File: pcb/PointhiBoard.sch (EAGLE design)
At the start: 99 parts, among them IC1 MCP7940NMSOP8, IC2 ADP2303ARDZ-5.0, IC3 IRF7240, IC4 IRF7240, IC6 4052D, IC7 ADR02, J1 22-27-2021-02, Q1 BSS123, Q2 BSS123, Q3 BSS123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

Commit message: fix wrong adc-port, little layout modifies
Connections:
- removed net RA4: IC5.RA4/T0CKI/C1OUT, R26.2
- new net AN4: IC5.RA5/AN4/HLVDIN/C2OUT, R26.2
- net N$60: now also IC5.RE1/WRN_AN6; no longer IC5.RA5/AN4/HLVDIN/C2OUT
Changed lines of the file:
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@@
-</segment>
-</net>
-<net name="RA4" class="0">
-<segment>
-<pinref part="IC5" gate="G$1" pin="RA4/T0CKI/C1OUT"/>
-<wire x1="254" y1="-142.24" x2="223.52" y2="-142.24" width="0.1524" layer="91"/>
-<label x="223.52" y="-142.24" size="1.778" layer="95" rot="R180" xref="yes"/>
-</segment>
-<segment>
-<pinref part="R26" gate="G$1" pin="2"/>
-<wire x1="558.8" y1="-132.08" x2="553.72" y2="-132.08" width="0.1524" layer="91"/>
-<label x="553.72" y="-132.08" size="1.778" layer="95" rot="R180" xref="yes"/>
 </segment>
 </net>
@@
 <net name="N$60" class="0">
 <segment>
-<pinref part="IC5" gate="G$1" pin="RA5/AN4/HLVDIN/C2OUT"/>
-<wire x1="254" y1="-147.32" x2="223.52" y2="-147.32" width="0.1524" layer="91"/>
 <pinref part="R31" gate="G$1" pin="1"/>
-<wire x1="223.52" y1="-147.32" x2="223.52" y2="-172.72" width="0.1524" layer="91"/>
 <wire x1="223.52" y1="-172.72" x2="142.24" y2="-172.72" width="0.1524" layer="91"/>
 <wire x1="142.24" y1="-172.72" x2="142.24" y2="-170.18" width="0.1524" layer="91"/>
@@
 <wire x1="142.24" y1="-175.26" x2="142.24" y2="-172.72" width="0.1524" layer="91"/>
 <junction x="142.24" y="-172.72"/>
+<pinref part="IC5" gate="G$1" pin="RE1/WRN_AN6"/>
+<wire x1="254" y1="-157.48" x2="223.52" y2="-157.48" width="0.1524" layer="91"/>
+<wire x1="223.52" y1="-157.48" x2="223.52" y2="-172.72" width="0.1524" layer="91"/>
 </segment>
 </net>
@@
 </segment>
 </net>
+<net name="AN4" class="0">
+<segment>
+<pinref part="IC5" gate="G$1" pin="RA5/AN4/HLVDIN/C2OUT"/>
+<wire x1="254" y1="-147.32" x2="246.38" y2="-147.32" width="0.1524" layer="91"/>
+<label x="246.38" y="-147.32" size="1.778" layer="95" rot="R180" xref="yes"/>
+</segment>
+<segment>
+<pinref part="R26" gate="G$1" pin="2"/>
+<wire x1="558.8" y1="-132.08" x2="556.26" y2="-132.08" width="0.1524" layer="91"/>
+<label x="556.26" y="-132.08" size="1.778" layer="95" rot="R180" xref="yes"/>
+</segment>
+</net>

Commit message: fix position and orentation of text(values, names,...) on the pcb
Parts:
- F1: value FUSESHK20L_6A -> 6A
- IC1: value MCP7940NMSOP8 -> MCP7940N
- IC5: value (none) -> 18F4420
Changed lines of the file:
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@@
 <?xml version="1.0" encoding="utf-8"?>
 <!DOCTYPE eagle SYSTEM "eagle.dtd">
-<eagle version="6.4">
+<eagle version="6.5.0">
 <drawing>
 <settings>
@@
 <part name="P+7" library="supply1" deviceset="V+" device=""/>
 <part name="R16" library="resistor" deviceset="R-EU_" device="R0805" value="10k"/>
-<part name="F1" library="fuse" deviceset="FUSE" device="SHK20L" value="FUSESHK20L_6A">
+<part name="F1" library="fuse" deviceset="FUSE" device="SHK20L" value="6A">
 <attribute name="MF" value=""/>
 <attribute name="MPN" value=""/>
@@
 <part name="R6" library="resistor" deviceset="R-EU_" device="R0805" value="10k"/>
 <part name="P+5" library="supply1" deviceset="+5V" device=""/>
-<part name="IC1" library="libsRobocup" deviceset="MCP7940N" device="MSOP8"/>
+<part name="IC1" library="libsRobocup" deviceset="MCP7940N" device="MSOP8" value="MCP7940N"/>
 <part name="32.768KHZ" library="crystal" deviceset="CRYSTAL" device="MM20SS"/>
 <part name="C1" library="resistor" deviceset="C-EU" device="C0805" value="10p"/>
@@
 <part name="P+6" library="supply1" deviceset="V+" device=""/>
 <part name="SUPPLY7" library="supply2" deviceset="+5V/1" device=""/>
-<part name="IC5" library="libsRobocup" deviceset="PIC18F4420" device=""/>
+<part name="IC5" library="libsRobocup" deviceset="PIC18F4420" device="" value="18F4420"/>
 <part name="SV1" library="con-harting-ml" deviceset="ML14" device="-3ML"/>
 <part name="GND12" library="supply1" deviceset="GND" device=""/>

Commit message: fix hole-diameter of con-harting-ml
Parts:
- SV1: value (none) -> D-IO; device con-harting-ml:ML14-3ML -> con-harting-ml-mod:ML14-3ML
- SV2: device con-harting-ml:ML10-3ML -> con-harting-ml-mod:ML10-3ML
- SV4: value (none) -> ADC-IN; device con-harting-ml:ML14-3ML -> con-harting-ml-mod:ML14-3ML
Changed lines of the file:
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@@
 <parts>
 <part name="U$1" library="RaspberryPi" deviceset="RASPBERRY-PI_REV2" device=""/>
-<part name="SV2" library="con-harting-ml" deviceset="ML10" device="-3ML" value="I2C"/>
+<part name="SV2" library="con-harting-ml-mod" deviceset="ML10" device="-3ML" value="I2C"/>
 <part name="Q1" library="transistor-small-signal" deviceset="BSS123" device=""/>
 <part name="Q2" library="transistor-small-signal" deviceset="BSS123" device=""/>
@@
 <part name="SUPPLY7" library="supply2" deviceset="+5V/1" device=""/>
 <part name="IC5" library="libsRobocup" deviceset="PIC18F4420" device="" value="18F4420"/>
-<part name="SV1" library="con-harting-ml" deviceset="ML14" device="-3ML"/>
+<part name="SV1" library="con-harting-ml-mod" deviceset="ML14" device="-3ML" value="D-IO"/>
 <part name="GND12" library="supply1" deviceset="GND" device=""/>
 <part name="P+8" library="supply1" deviceset="+5V" device=""/>
@@
 <part name="R11" library="resistor" deviceset="R-EU_" device="R0805" value="330R"/>
 <part name="R12" library="resistor" deviceset="R-EU_" device="R0805" value="330R"/>
-<part name="SV4" library="con-harting-ml" deviceset="ML14" device="-3ML"/>
+<part name="SV4" library="con-harting-ml-mod" deviceset="ML14" device="-3ML" value="ADC-IN"/>
 <part name="IC6" library="40xx" deviceset="4052" device="D"/>
 <part name="GND23" library="supply1" deviceset="GND" device=""/>

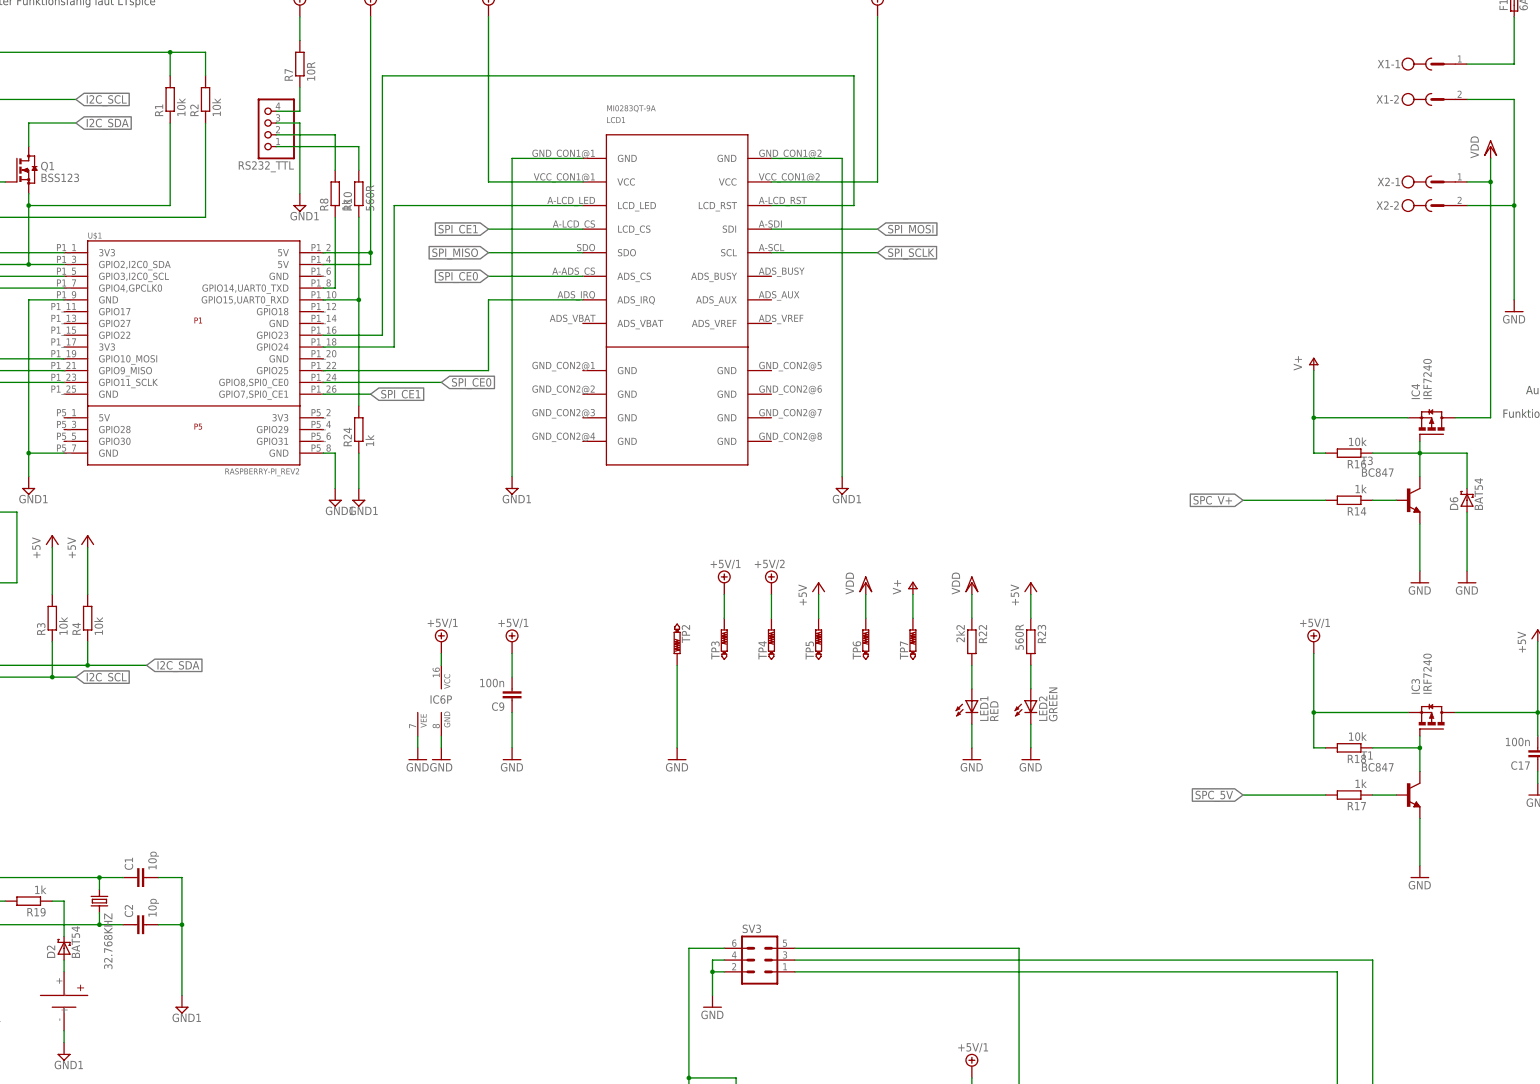
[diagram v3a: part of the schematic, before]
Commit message: fix warnings on pcb
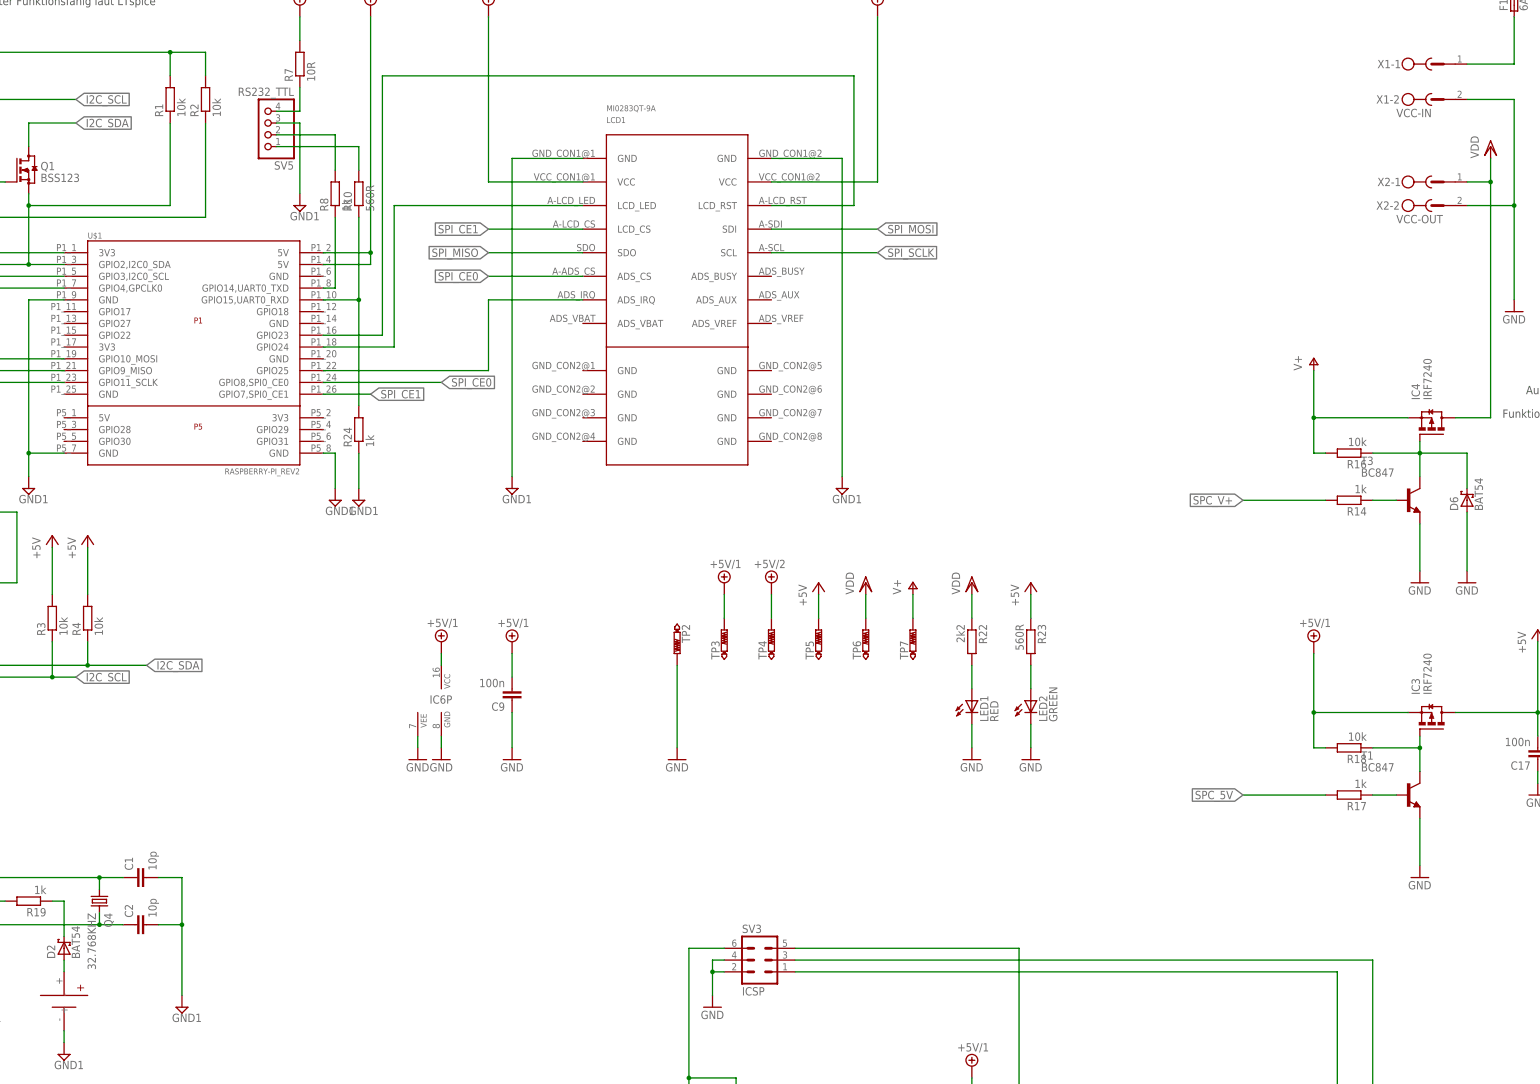
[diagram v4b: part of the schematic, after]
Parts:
- Q4: value (none) -> 32.768KHZ
- SV3: value (none) -> ICSP
- SV5: value (none) -> RS232_TTL
- X1: value (none) -> VCC-IN
- X2: value (none) -> VCC-OUT
- renumbered 32.768KHZ to Q4, RS232_TTL to SV5
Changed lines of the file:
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@@
 <part name="P+1" library="supply1" deviceset="+5V" device=""/>
 <part name="VDD1" library="supply1" deviceset="VDD" device=""/>
-<part name="X1" library="con-phoenix-500" deviceset="MSTBV2" device=""/>
-<part name="X2" library="con-phoenix-500" deviceset="MSTBV2" device=""/>
+<part name="X1" library="con-phoenix-500" deviceset="MSTBV2" device="" value="VCC-IN"/>
+<part name="X2" library="con-phoenix-500" deviceset="MSTBV2" device="" value="VCC-OUT"/>
 <part name="GND4" library="supply1" deviceset="GND" device=""/>
 <part name="P+2" library="supply1" deviceset="V+" device=""/>
@@
 <part name="P+5" library="supply1" deviceset="+5V" device=""/>
 <part name="IC1" library="libsRobocup" deviceset="MCP7940N" device="MSOP8" value="MCP7940N"/>
-<part name="32.768KHZ" library="crystal" deviceset="CRYSTAL" device="MM20SS"/>
+<part name="Q4" library="crystal" deviceset="CRYSTAL" device="MM20SS" value="32.768KHZ"/>
 <part name="C1" library="resistor" deviceset="C-EU" device="C0805" value="10p"/>
 <part name="C2" library="resistor" deviceset="C-EU" device="C0805" value="10p"/>
@@
 <part name="J1" library="con-molex" deviceset="22-?-02" device="27-2021"/>
 <part name="GND39" library="supply1" deviceset="GND" device=""/>
-<part name="RS232_TTL" library="pinhead" deviceset="PINHD-1X4" device=""/>
+<part name="SV5" library="pinhead" deviceset="PINHD-1X4" device="" value="RS232_TTL"/>
 <part name="SUPPLY6" library="supply2" deviceset="+5V/2" device=""/>
 <part name="R7" library="resistor" deviceset="R-EU_" device="R0805" value="10R"/>
@@
 <part name="GND21" library="supply1" deviceset="GND" device=""/>
 <part name="SJ2" library="jumper" deviceset="SJ" device=""/>
-<part name="SV3" library="con-harting-ml" deviceset="ML6" device=""/>
+<part name="SV3" library="con-harting-ml" deviceset="ML6" device="" value="ICSP"/>
 <part name="GND22" library="supply1" deviceset="GND" device=""/>
 <part name="D3" library="diode" deviceset="BAT54" device=""/>
@@
 <instance part="P+5" gate="1" x="10.16" y="35.56"/>
 <instance part="IC1" gate="G$1" x="10.16" y="-55.88"/>
-<instance part="32.768KHZ" gate="G$1" x="60.96" y="-45.72" rot="R270"/>
+<instance part="Q4" gate="G$1" x="60.96" y="-45.72" rot="R270"/>
 <instance part="C1" gate="G$1" x="68.58" y="-40.64" rot="R90"/>
 <instance part="C2" gate="G$1" x="68.58" y="-50.8" rot="R90"/>
@@
 <instance part="J1" gate="-2" x="386.08" y="-10.16"/>
 <instance part="GND39" gate="1" x="381" y="-22.86"/>
-<instance part="RS232_TTL" gate="A" x="96.52" y="121.92" rot="R180"/>
+<instance part="SV5" gate="A" x="96.52" y="121.92" rot="R180"/>
 <instance part="SUPPLY6" gate="G$1" x="104.14" y="147.32"/>
 <instance part="R7" gate="G$1" x="104.14" y="134.62" rot="R90"/>
@@
 <pinref part="C1" gate="G$1" pin="1"/>
 <wire x1="66.04" y1="-40.64" x2="60.96" y2="-40.64" width="0.1524" layer="91"/>
-<pinref part="32.768KHZ" gate="G$1" pin="1"/>
+<pinref part="Q4" gate="G$1" pin="1"/>
 <wire x1="60.96" y1="-40.64" x2="25.4" y2="-40.64" width="0.1524" layer="91"/>
 <wire x1="60.96" y1="-43.18" x2="60.96" y2="-40.64" width="0.1524" layer="91"/>
@@
 <pinref part="C2" gate="G$1" pin="1"/>
 <wire x1="66.04" y1="-50.8" x2="60.96" y2="-50.8" width="0.1524" layer="91"/>
-<pinref part="32.768KHZ" gate="G$1" pin="2"/>
+<pinref part="Q4" gate="G$1" pin="2"/>
 <wire x1="60.96" y1="-50.8" x2="25.4" y2="-50.8" width="0.1524" layer="91"/>
 <wire x1="60.96" y1="-48.26" x2="60.96" y2="-50.8" width="0.1524" layer="91"/>
@@
 <net name="N$8" class="0">
 <segment>
-<pinref part="RS232_TTL" gate="A" pin="4"/>
+<pinref part="SV5" gate="A" pin="4"/>
 <wire x1="99.06" y1="124.46" x2="104.14" y2="124.46" width="0.1524" layer="91"/>
 <pinref part="R7" gate="G$1" pin="1"/>
@@
 <net name="N$10" class="0">
 <segment>
-<pinref part="RS232_TTL" gate="A" pin="2"/>
+<pinref part="SV5" gate="A" pin="2"/>
 <pinref part="R8" gate="G$1" pin="2"/>
 <wire x1="99.06" y1="119.38" x2="111.76" y2="119.38" width="0.1524" layer="91"/>
@@
 <net name="N$57" class="0">
 <segment>
-<pinref part="RS232_TTL" gate="A" pin="1"/>
+<pinref part="SV5" gate="A" pin="1"/>
 <pinref part="R10" gate="G$1" pin="2"/>
 <wire x1="99.06" y1="116.84" x2="116.84" y2="116.84" width="0.1524" layer="91"/>
@@
 </segment>
 <segment>
-<pinref part="RS232_TTL" gate="A" pin="3"/>
+<pinref part="SV5" gate="A" pin="3"/>
 <wire x1="99.06" y1="121.92" x2="104.14" y2="121.92" width="0.1524" layer="91"/>
 <wire x1="104.14" y1="121.92" x2="104.14" y2="106.68" width="0.1524" layer="91"/>
@@
 </sheet>
 </sheets>
+<errors>
+</errors>
 </schematic>
 </drawing>

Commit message: update pcb
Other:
- note removed: "I2C-Sp.-Konverter Funktionsfähig laut LTspice"
- moved on the sheet: R3, R4, R6, SJ1, SV2
